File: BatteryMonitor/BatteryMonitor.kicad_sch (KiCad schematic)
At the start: 60 parts, among them J1 SWD, J2 BAT+, J3 BAL_THERM, J4 I2C, J5 BAT-, J6 PACK_OUT, Q1 NTMFS0D6N04XM, Q2 NTMFS0D6N04XM, SW1 WAKE, U1 BQ76905, U2 STM32L071KZUx

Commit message: BatteryMonitor added power switch connector
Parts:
- added J7: PWR_SWITCH, BW_Connectors:Amphenol_MINITEK_WTB_1.25_2P, symbol Connector:Conn_01x02_Pin
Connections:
- net GND: now also J7.2 (Pin_2)
- net PWR_SWITCH: now reaches U2.1 (PC14)
- net PWR_SWITCH: now also J7.1 (Pin_1)
- no-connect marks 16 -> 15
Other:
- moved on the sheet: C22, D3, R18, SW1

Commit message: BatteryMonitor v1.1: I2C swap, isolation
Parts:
- added C11, C16: 0.1µF, Capacitor_SMD:C_0603_1608Metric, symbol Device:C_Small
- added C12, C19: 1nF, Capacitor_SMD:C_0603_1608Metric, symbol Device:C_Small
- added Q1: NX138BK, Package_TO_SOT_SMD:SOT-23-3, symbol Device:Q_NMOS_GSD
- added R13: 1MΩ, Resistor_SMD:R_0603_1608Metric, symbol Device:R_Small_US
- added R7, R8: 10kΩ, Resistor_SMD:R_0603_1608Metric, symbol Device:R_Small_US
- added U3: ADuM1252, Package_SO:MSOP-8_3x3mm_P0.65mm, symbol BW_Active:ADuM1252
- renumbered C11 to C13, C12 to C14, C13 to C15, C14 to C17, C15 to C18, C16 to C20, C17 to C21, C18 to C22, C19 to C23, C20 to C24, C21 to C25, C22 to C26, Q1 to Q2, Q2 to Q3, R8 to R10, R9 to R11, R10 to R12, R11 to R14, R12 to R15, R13 to R16, R14 to R17, R15 to R18, R16 to R19, R17 to R20, R18 to R21, R7 to R9
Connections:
- net +3.3V: now also C16.2, C19.2, R7.1, R8.1, U3.1 (VDD1)
- net GND: now also Q1.2 (S), R13.2; no longer J4.4 (Pin_4)
- net SCL_BMS: now reaches R4.2, TP4.1, U1.12 (SCL)
- net SCL_BMS: now also U2.18 (PA8); no longer U2.28 (PB6)
- net at R3.2, TP3.1, U1.13 (SDA): now also U2.26 (PB4); no longer U2.29 (PB7)
- net at J4.1 (Pin_1): now also C11.1, C12.1, U3.8 (VDD2); no longer U2.18 (PA8)
- net at U2.19 (PA9): now also Q1.1 (G), R13.1; no longer J4.3 (Pin_3)
- net SDA_EXT: no longer names the net of J4.2 (Pin_2)
- net SDA_EXT: now also U3.7 (SDA2); no longer U2.26 (PB4)
- new net: C16.1, C19.1, Q1.3 (D), U3.4 (GND1)
- new net: J4.3 (Pin_3), U3.6 (SCL2)
- new net GNDEXT: C11.2, C12.2, J4.4 (Pin_4), U3.5 (GND2)
- new net SCL_ISO: R7.2, U2.28 (PB6), U3.3 (SCL1)
- new net SDA_ISO: R8.2, U2.29 (PB7), U3.2 (SDA1)
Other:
- moved on the sheet: C1, C10, C13, C14, C15, C17, C18, C2, C20, C21, C22, C23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

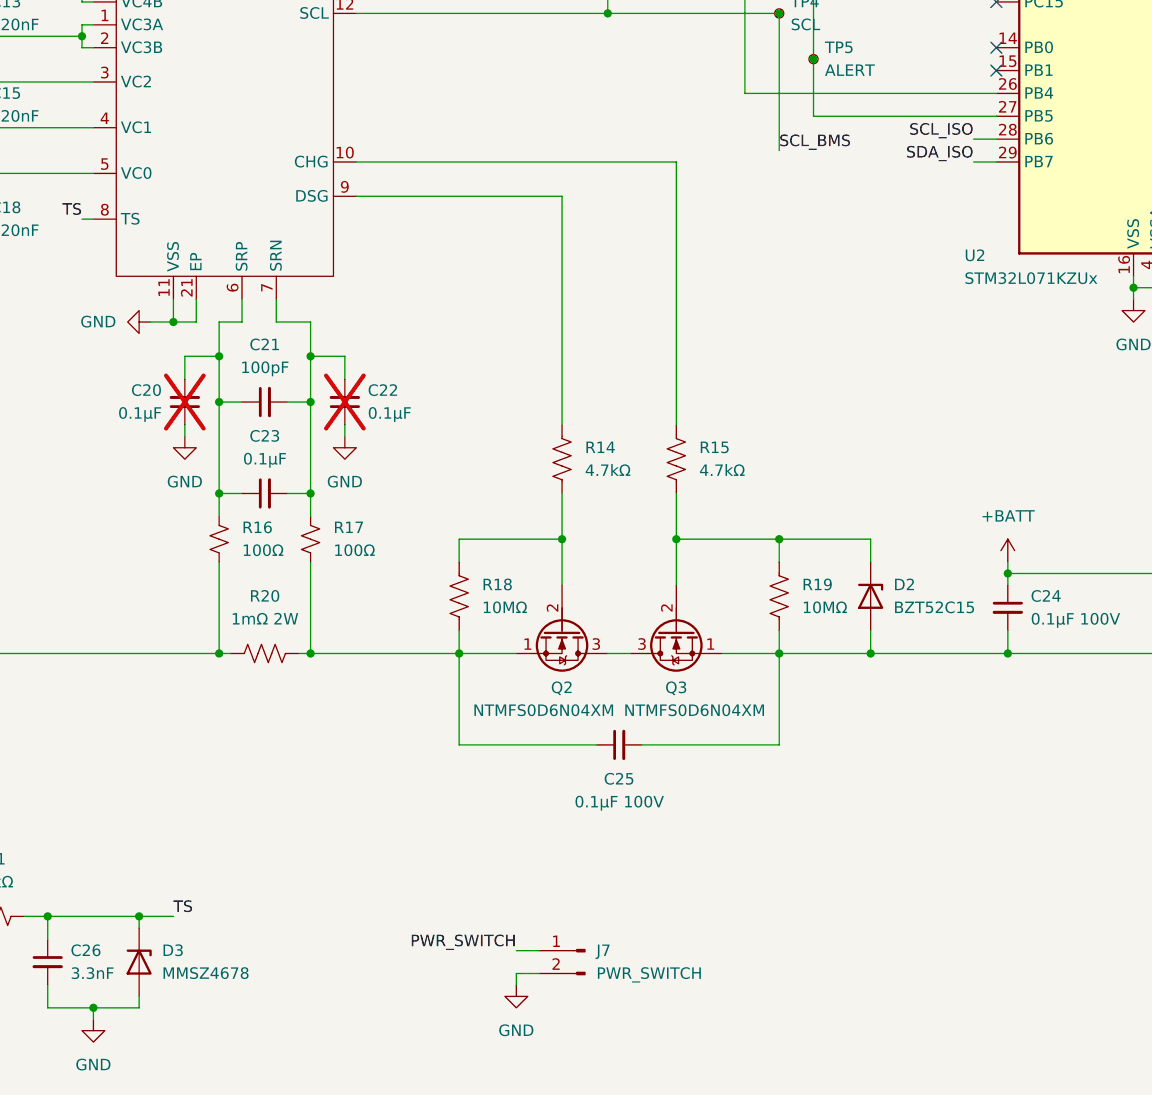
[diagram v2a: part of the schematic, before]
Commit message: BatteryMonitor doubled FET protection zener
Single zener causes excessive leakage when off; opposite-polarity pair fixes that
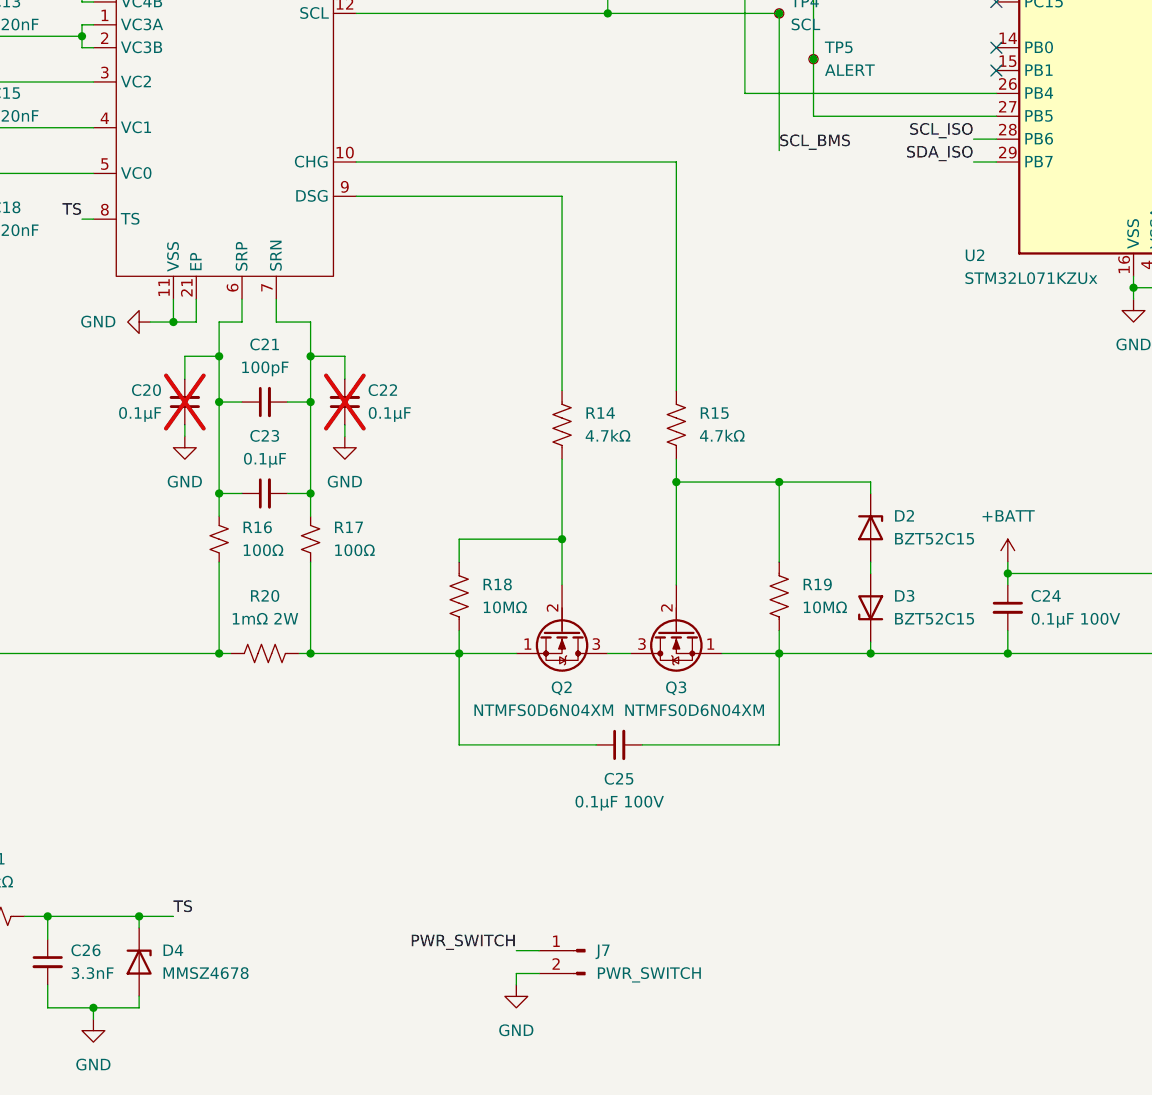
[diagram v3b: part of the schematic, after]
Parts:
- added D3: BZT52C15, Diode_SMD:D_SOD-123, symbol Device:D_Zener
- renumbered D3 to D4
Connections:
- net at C24.2, C25.2, J6.1 (Pin_1)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: now also D3.1 (K); no longer D2.2 (A)
- new net: D2.2 (A), D3.2 (A)
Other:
- moved on the sheet: D2, R14, R15
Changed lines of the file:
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@@
 	(paper "A4")
 	(junction
+		(at 144.78 115.57)
+		(diameter 0)
+		(color 0 0 0 0)
+	)
+	(junction
 		(at 240.03 78.74)
 		(diameter 0)
@@
 	)
 	(junction
-		(at 144.78 121.92)
-		(diameter 0)
-		(color 0 0 0 0)
-	)
-	(junction
 		(at 39.37 55.88)
 		(diameter 0)
@@
 	)
 	(junction
+		(at 166.37 134.62)
+		(diameter 0)
+		(color 0 0 0 0)
+	)
+	(junction
 		(at 120.65 134.62)
 		(diameter 0)
@@
 	)
 	(junction
-		(at 156.21 121.92)
+		(at 156.21 115.57)
 		(diameter 0)
 		(color 0 0 0 0)
@@
 	)
 	(junction
-		(at 166.37 134.62)
-		(diameter 0)
-		(color 0 0 0 0)
-	)
-	(junction
 		(at 104.14 106.68)
 		(diameter 0)
@@
 	(wire
 		(pts
-			(xy 166.37 134.62) (xy 156.21 134.62)
+			(xy 156.21 134.62) (xy 166.37 134.62)
 		)
 		(stroke
@@
 	(wire
 		(pts
-			(xy 144.78 80.01) (xy 144.78 109.22)
+			(xy 144.78 80.01) (xy 144.78 105.41)
 		)
 		(stroke
@@
 	(wire
 		(pts
-			(xy 156.21 121.92) (xy 144.78 121.92)
+			(xy 156.21 115.57) (xy 144.78 115.57)
 		)
 		(stroke
@@
 	(wire
 		(pts
+			(xy 166.37 134.62) (xy 181.61 134.62)
+		)
+		(stroke
+			(width 0)
+			(type default)
+		)
+	)
+	(wire
+		(pts
 			(xy 160.02 55.88) (xy 160.02 68.58)
 		)
@@
 	(wire
 		(pts
-			(xy 156.21 124.46) (xy 156.21 121.92)
-		)
-		(stroke
-			(width 0)
-			(type default)
-		)
-	)
-	(wire
-		(pts
 			(xy 60.96 91.44) (xy 63.5 91.44)
 		)
@@
 	(wire
 		(pts
-			(xy 144.78 121.92) (xy 144.78 127)
-		)
-		(stroke
-			(width 0)
-			(type default)
-		)
-	)
-	(wire
-		(pts
 			(xy 38.1 71.12) (xy 49.53 71.12)
 		)
@@
 	(wire
 		(pts
-			(xy 144.78 116.84) (xy 144.78 121.92)
+			(xy 144.78 113.03) (xy 144.78 115.57)
 		)
 		(stroke
@@
 	(wire
 		(pts
-			(xy 166.37 134.62) (xy 181.61 134.62)
+			(xy 233.68 57.15) (xy 210.82 57.15)
 		)
 		(stroke
@@
 	(wire
 		(pts
-			(xy 233.68 57.15) (xy 210.82 57.15)
+			(xy 153.67 27.94) (xy 153.67 29.21)
 		)
 		(stroke
@@
 	(wire
 		(pts
-			(xy 153.67 27.94) (xy 153.67 29.21)
+			(xy 144.78 115.57) (xy 144.78 127)
 		)
 		(stroke
@@
 	(wire
 		(pts
+			(xy 166.37 115.57) (xy 166.37 116.84)
+		)
+		(stroke
+			(width 0)
+			(type default)
+		)
+	)
+	(wire
+		(pts
 			(xy 195.58 41.91) (xy 198.12 41.91)
 		)
@@
 	(wire
 		(pts
-			(xy 132.08 116.84) (xy 132.08 121.92)
+			(xy 132.08 113.03) (xy 132.08 121.92)
 		)
 		(stroke
@@
 	(wire
 		(pts
-			(xy 166.37 124.46) (xy 166.37 121.92)
-		)
-		(stroke
-			(width 0)
-			(type default)
-		)
-	)
-	(wire
-		(pts
 			(xy 74.93 163.83) (xy 74.93 166.37)
 		)
@@
 	(wire
 		(pts
-			(xy 132.08 83.82) (xy 132.08 109.22)
+			(xy 132.08 83.82) (xy 132.08 105.41)
 		)
 		(stroke
@@
 	(wire
 		(pts
-			(xy 166.37 132.08) (xy 166.37 134.62)
-		)
-		(stroke
-			(width 0)
-			(type default)
-		)
-	)
-	(wire
-		(pts
 			(xy 109.22 55.88) (xy 116.84 55.88)
 		)
@@
 	(wire
 		(pts
-			(xy 166.37 121.92) (xy 156.21 121.92)
+			(xy 166.37 115.57) (xy 156.21 115.57)
 		)
 		(stroke
@@
 	(wire
 		(pts
+			(xy 166.37 124.46) (xy 166.37 125.73)
+		)
+		(stroke
+			(width 0)
+			(type default)
+		)
+	)
+	(wire
+		(pts
 			(xy 190.5 31.75) (xy 191.77 31.75)
 		)
@@
 	(wire
 		(pts
+			(xy 156.21 115.57) (xy 156.21 124.46)
+		)
+		(stroke
+			(width 0)
+			(type default)
+		)
+	)
+	(wire
+		(pts
 			(xy 93.98 106.68) (xy 96.52 106.68)
 		)
@@
 	(wire
 		(pts
+			(xy 166.37 133.35) (xy 166.37 134.62)
+		)
+		(stroke
+			(width 0)
+			(type default)
+		)
+	)
+	(wire
+		(pts
 			(xy 59.69 39.37) (xy 67.31 39.37)
 		)
@@
 	(symbol
 		(lib_id "Device:R_US")
-		(at 144.78 113.03 0)
+		(at 144.78 109.22 0)
 		(unit 1)
 		(exclude_from_sim no)
@@
 		(fields_autoplaced yes)
 		(property "Reference" "R15"
-			(at 147.32 111.7599 0)
+			(at 147.32 107.9499 0)
 			(effects
 				(font
@@
 		)
 		(property "Value" "4.7kΩ"
-			(at 147.32 114.2999 0)
+			(at 147.32 110.4899 0)
 			(effects
 				(font
@@
 		)
 		(property "Footprint" "Resistor_SMD:R_0603_1608Metric"
-			(at 145.796 113.284 90)
+			(at 145.796 109.474 90)
 			(effects
 				(font
@@
 		)
 		(property "Datasheet" "~"
-			(at 144.78 113.03 0)
+			(at 144.78 109.22 0)
 			(effects
 				(font
@@
 		)
 		(property "Description" "Resistor, US symbol"
-			(at 144.78 113.03 0)
+			(at 144.78 109.22 0)
 			(effects
 				(font
@@
 	)
 	(symbol
+		(lib_id "Device:D_Zener")
+		(at 166.37 129.54 90)
+		(unit 1)
+		(exclude_from_sim no)
+		(in_bom yes)
+		(on_board yes)
+		(dnp no)
+		(fields_autoplaced yes)
+		(property "Reference" "D3"
+			(at 168.91 128.2699 90)
+			(effects
+				(font
+					(size 1.27 1.27)
+				)
+				(justify right)
+			)
+		)
+		(property "Value" "BZT52C15"
+			(at 168.91 130.8099 90)
+			(effects
+				(font
+					(size 1.27 1.27)
+				)
+				(justify right)
+			)
+		)
+		(property "Footprint" "Diode_SMD:D_SOD-123"
+			(at 166.37 129.54 0)
+			(effects
+				(font
+					(size 1.27 1.27)
+				)
+				(hide yes)
+			)
+		)
+		(property "Datasheet" "~"
+			(at 166.37 129.54 0)
+			(effects
+				(font
+					(size 1.27 1.27)
+				)
+				(hide yes)
+			)
+		)
+		(property "Description" "Zener diode"
+			(at 166.37 129.54 0)
+			(effects
+				(font
+					(size 1.27 1.27)
+				)
+				(hide yes)
+			)
+		)
+		(pin "2"
+		)
+		(pin "1"
+		)
+		(instances
+			(project "BatteryMonitor"
+				(path "/9402596f-ffe7-4317-a9ce-fac462627500"
+					(reference "D3")
+					(unit 1)
+				)
+			)
+		)
+	)
+	(symbol
 		(lib_id "Connector:TestPoint_Small")
 		(at 156.21 63.5 0)
@@
 	(symbol
 		(lib_id "Device:D_Zener")
-		(at 166.37 128.27 270)
+		(at 166.37 120.65 270)
 		(unit 1)
 		(exclude_from_sim no)
@@
 		(fields_autoplaced yes)
 		(property "Reference" "D2"
-			(at 168.91 126.9999 90)
+			(at 168.91 119.3799 90)
 			(effects
 				(font
@@
 		)
 		(property "Value" "BZT52C15"
-			(at 168.91 129.5399 90)
+			(at 168.91 121.9199 90)
 			(effects
 				(font
@@
 		)
 		(property "Footprint" "Diode_SMD:D_SOD-123"
-			(at 166.37 128.27 0)
+			(at 166.37 120.65 0)
 			(effects
 				(font
@@
 		)
 		(property "Datasheet" "~"
-			(at 166.37 128.27 0)
+			(at 166.37 120.65 0)
 			(effects
 				(font
@@
 		)
 		(property "Description" "Zener diode"
-			(at 166.37 128.27 0)
+			(at 166.37 120.65 0)
 			(effects
 				(font
@@
 		(dnp no)
 		(fields_autoplaced yes)
-		(property "Reference" "D3"
+		(property "Reference" "D4"
 			(at 87.63 167.6399 90)
 			(effects
@@
 			(project "BatteryMonitor"
 				(path "/9402596f-ffe7-4317-a9ce-fac462627500"
-					(reference "D3")
+					(reference "D4")
 					(unit 1)
 				)
@@
 	(symbol
 		(lib_id "Device:R_US")
-		(at 132.08 113.03 0)
+		(at 132.08 109.22 0)
 		(unit 1)
 		(exclude_from_sim no)
@@
 		(fields_autoplaced yes)
 		(property "Reference" "R14"
-			(at 134.62 111.7599 0)
+			(at 134.62 107.9499 0)
 			(effects
 				(font
@@
 		)
 		(property "Value" "4.7kΩ"
-			(at 134.62 114.2999 0)
+			(at 134.62 110.4899 0)
 			(effects
 				(font
@@
 		)
 		(property "Footprint" "Resistor_SMD:R_0603_1608Metric"
-			(at 133.096 113.284 90)
+			(at 133.096 109.474 90)
 			(effects
 				(font
@@
 		)
 		(property "Datasheet" "~"
-			(at 132.08 113.03 0)
+			(at 132.08 109.22 0)
 			(effects
 				(font
@@
 		)
 		(property "Description" "Resistor, US symbol"
-			(at 132.08 113.03 0)
+			(at 132.08 109.22 0)
 			(effects
 				(font
